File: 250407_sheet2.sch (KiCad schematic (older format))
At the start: 90 parts, among them CN5 AV_CONN, CN6 EXPANSION_PORT, M1 MODULATOR_LONGBOARD, Q8 2SC1815, U10 4164-2, U11 4164-2, U12 4164-2, U13 74LS257, U14 74LS258, U15 74LS139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

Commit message: replaced CR5, CR6, F1 and CN10 with symbols closer to original schematics
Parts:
- CN5: symbol 250407_-rescue:AV_CONN-KU-schematics-library -> KU-schematics-library:AV_CONN
- CN6: symbol 250407_-rescue:EXPANSION_PORT-KU-schematics-library -> KU-schematics-library:EXPANSION_PORT
- FB10, FB11, FB12, FB13, FB14, FB15, FB22, FB4: symbol 250407_-rescue:FERRITE_BEAD-KU-schematics-library -> KU-schematics-library:FERRITE_BEAD
- RP1, RP2: symbol 250407_-rescue:R_ARRAY_US_4RES-KU-schematics-library -> KU-schematics-library:R_ARRAY_US_4RES
- U10, U11, U12, U21, U22, U23, U24, U9: symbol 250407_-rescue:4164-2-KU-schematics-library -> KU-schematics-library:4164-2
- U13: symbol 250407_-rescue:74LS257_U13-KU-schematics-library -> KU-schematics-library:74LS257_U13
- U14: symbol 250407_-rescue:74LS258-KU-schematics-library -> KU-schematics-library:74LS258
- U16: symbol 250407_-rescue:4066_U28-KU-schematics-library -> KU-schematics-library:4066_U28
- U18: symbol 250407_-rescue:SID-KU-schematics-library -> KU-schematics-library:SID
- U19: symbol 250407_-rescue:VIC-KU-schematics-library -> KU-schematics-library:VIC
- U25: symbol 250407_-rescue:74LS257-KU-schematics-library -> KU-schematics-library:74LS257
- U26: symbol 250407_-rescue:74LS373-KU-schematics-library -> KU-schematics-library:74LS373
- U27: symbol 250407_-rescue:7408_U27-KU-schematics-library -> KU-schematics-library:7408_U27
- U3, U4: symbol 250407_-rescue:2364A_ROM-KU-schematics-library -> KU-schematics-library:2364A_ROM
- U5: symbol 250407_-rescue:2332A_ROM-KU-schematics-library -> KU-schematics-library:2332A_ROM

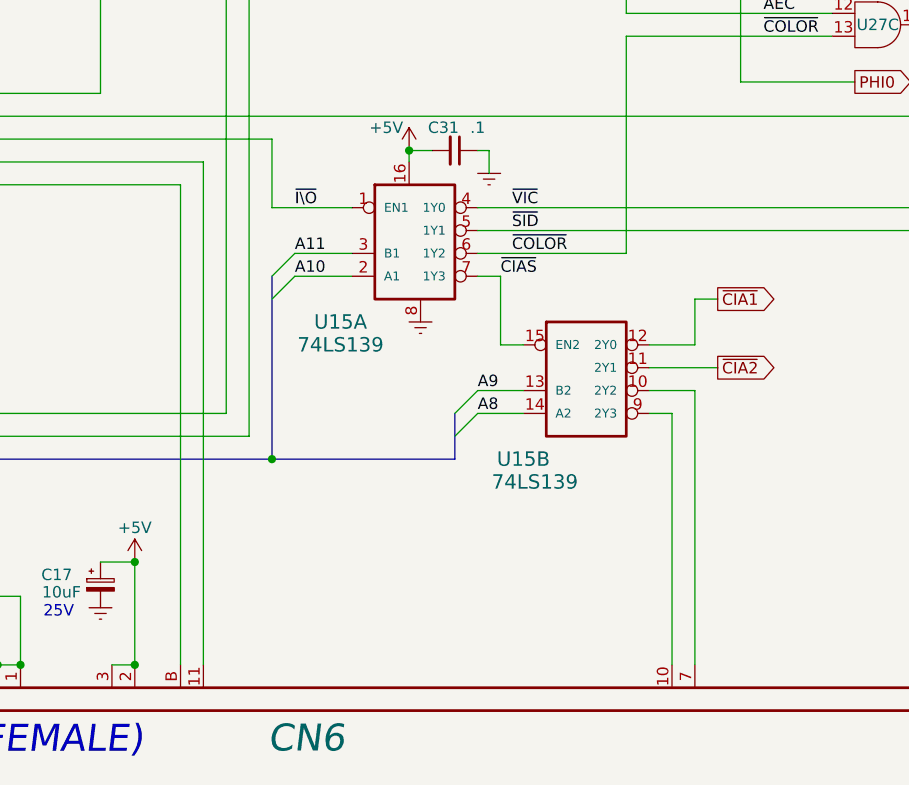
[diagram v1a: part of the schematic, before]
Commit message: add labels to ROML, ROMH, I/O1 and I/O2
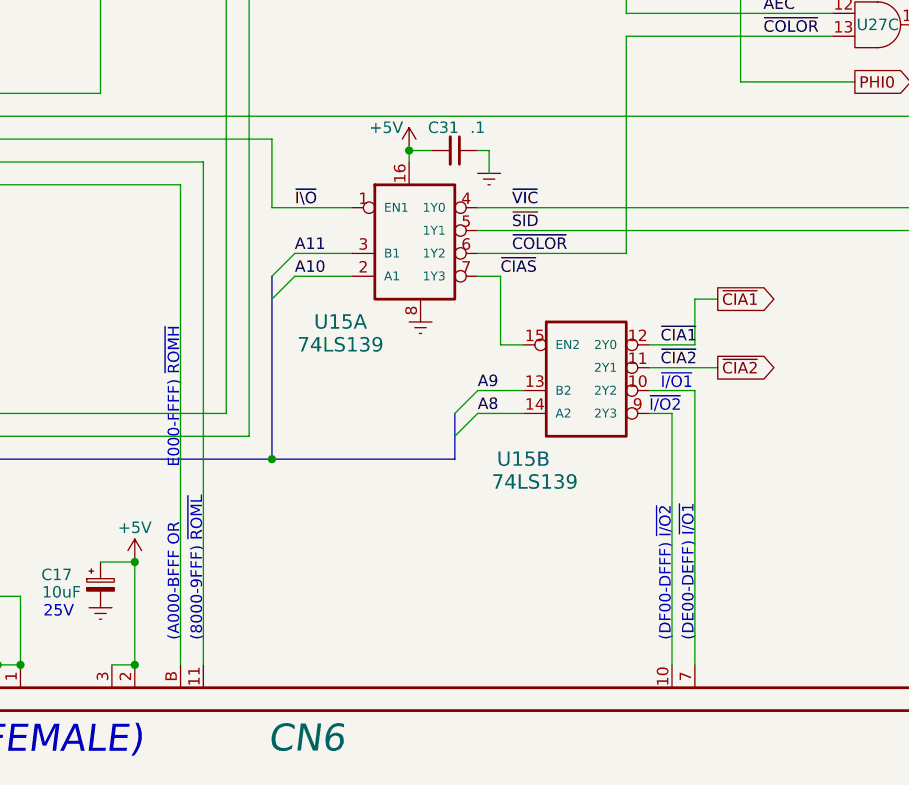
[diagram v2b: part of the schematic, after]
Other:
- note added: "(8000-9FFF) ~ROML~"
- note added: "(A000-BFFF OR E000-FFFF) ~ROMH~"
- note added: "(DE00-DEFF) ~I/O1~"
- note added: "(DF00-DFFF) ~I/O2~"
- note added: "~I/O1~"
- note added: "~I/O2~"
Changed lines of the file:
@@
 	1    0    0    1
 $EndComp
+Text Notes 7200 10200 1    50   ~ 0
+(A000-BFFF OR           E000-FFFF) ~ROMH~
+Text Notes 7300 10200 1    50   ~ 0
+(8000-9FFF) ~ROML~
+Text Notes 9350 10200 1    50   ~ 0
+(DF00-DFFF) ~I/O2~
+Text Notes 9450 10200 1    50   ~ 0
+(DE00-DEFF) ~I/O1~
+Text Label 9300 8900 0    50   ~ 0
+~CIA1~
+Text Label 9300 9000 0    50   ~ 0
+~CIA2~
+Text Notes 9300 9100 0    50   ~ 0
+~I/O1~
+Text Notes 9250 9200 0    50   ~ 0
+~I/O2~
 Wire Bus Line
 	8400 9200 8400 9400
